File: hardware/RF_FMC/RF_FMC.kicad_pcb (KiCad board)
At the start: 4 copper layers, 84 x 69 mm, 32 parts, among them CN1 FMC_Mezzanine, Q1 SI1539CDL-T1-GE3, Q2 SI1539CDL-T1-GE3, Q3 SI1539CDL-T1-GE3, Q4 Si7141DP, Q5 Si7141DP, Q6 Si7141DP, U1 24LC024-I/SN

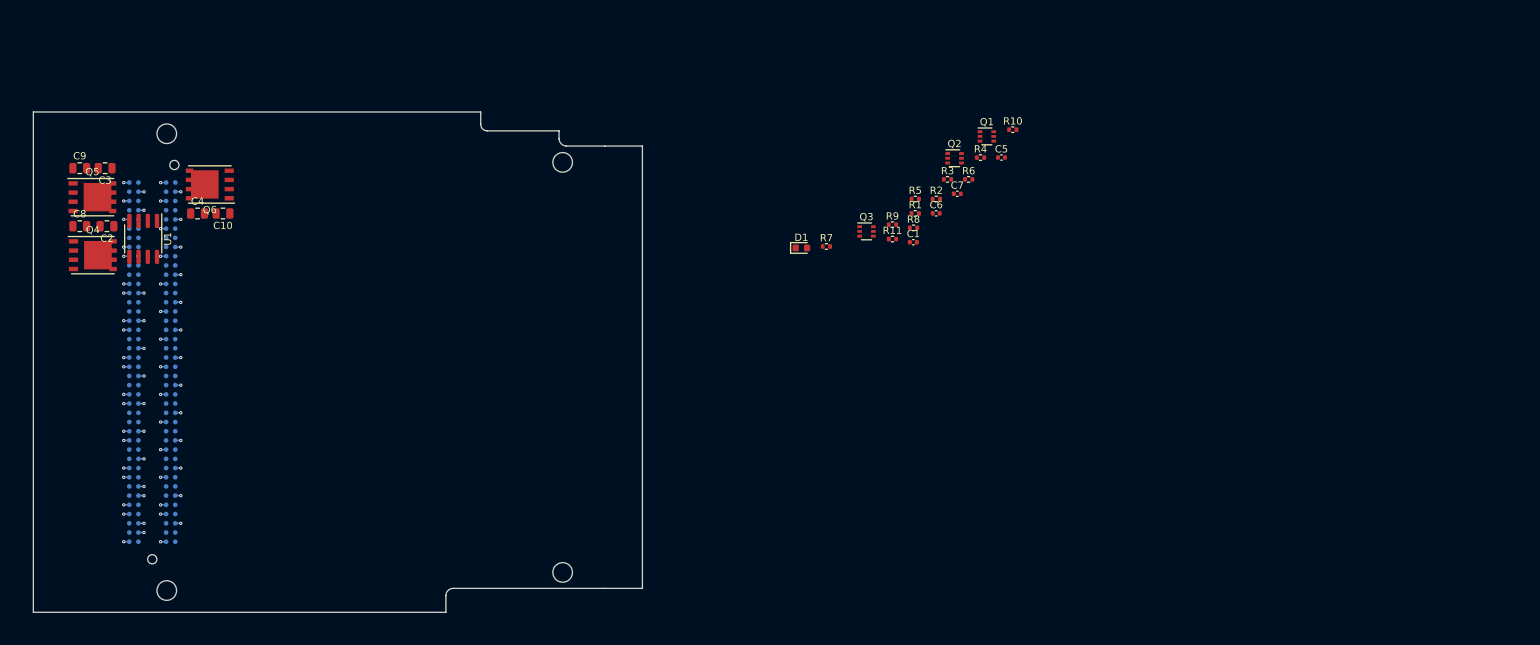
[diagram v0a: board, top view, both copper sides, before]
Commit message: Redid FMC template to parts I can actually buy!
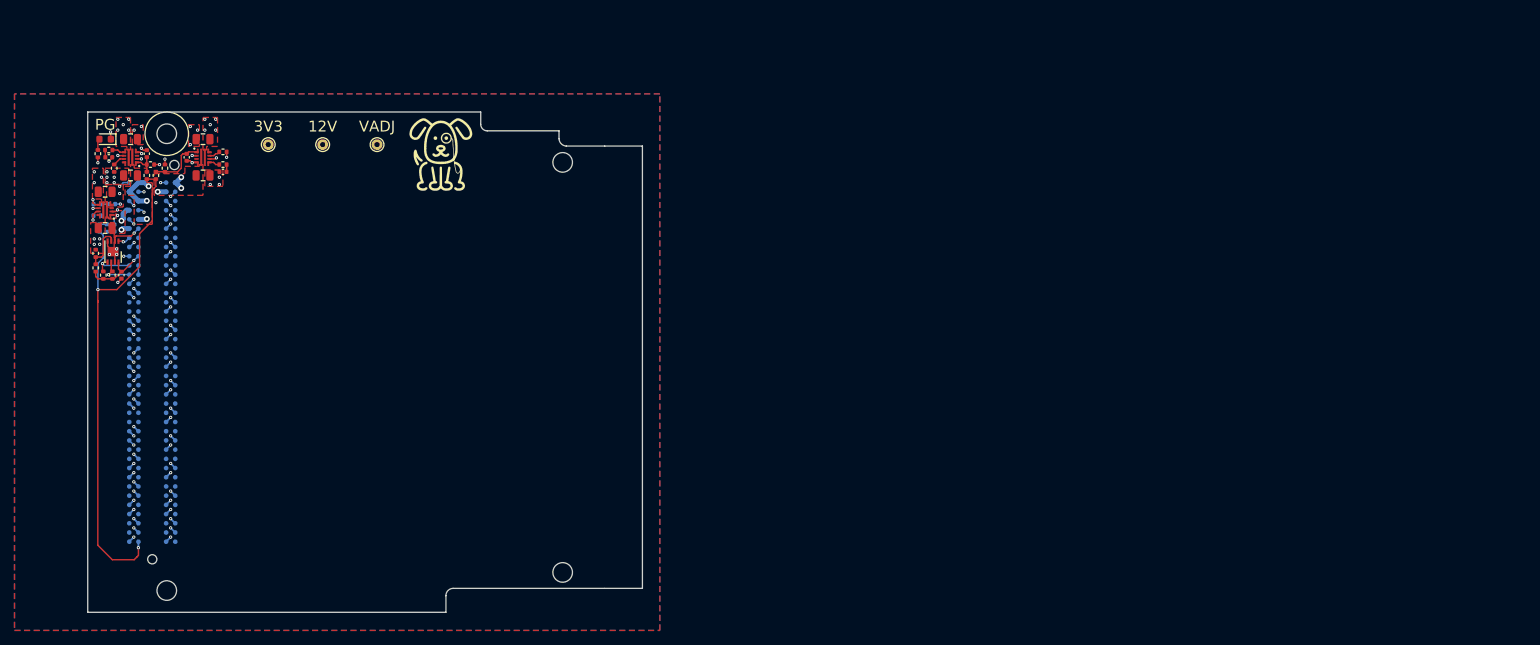
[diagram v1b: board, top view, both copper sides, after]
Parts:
- removed Q1, Q2, Q3: SI1539CDL-T1-GE3, Package_TO_SOT_SMD:SOT-363_SC-70-6
- removed Q4, Q5, Q6: Si7141DP, Package_SO:PowerPAK_SO-8_Single
- added C11: 10u, Capacitor_SMD:C_0805_2012Metric, F.Cu at (112.5, 76.5)
- added C12: 10u, Capacitor_SMD:C_0805_2012Metric, F.Cu at (116.0, 69.2)
- added C13: 10u, Capacitor_SMD:C_0805_2012Metric, F.Cu at (126.0, 69.2)
- added M1: Logo_10mmx10mm, Misc_WUT:Logo_10mmx10mm, F.Cu at (158.8, 71.5)
- added R12: 100, Resistor_SMD:R_0402_1005Metric, B.Cu at (111.4, 78.2)
- added R13: 100, Resistor_SMD:R_0402_1005Metric, F.Cu at (113.0, 70.8)
- added R14: 100, Resistor_SMD:R_0402_1005Metric, F.Cu at (128.8, 72.8)
- added R15: 2k, Resistor_SMD:R_0402_1005Metric, B.Cu at (111.4, 79.8)
- added R16: 2k, Resistor_SMD:R_0402_1005Metric, F.Cu at (113.8, 73.2)
- added R17: 2k, Resistor_SMD:R_0402_1005Metric, F.Cu at (128.8, 71.0)
- added TP1: TestPoint, TestPoint:TestPoint_THTPad_D1.5mm_Drill0.7mm, F.Cu at (142.5, 70.0)
- added TP2: TestPoint, TestPoint:TestPoint_THTPad_D1.5mm_Drill0.7mm, F.Cu at (135.0, 70.0)
- added TP3: TestPoint, TestPoint:TestPoint_THTPad_D1.5mm_Drill0.7mm, F.Cu at (150.0, 70.0)
- added U2: LM73100RPWR, IC_WUT:TI_LM73100_RPW, F.Cu at (112.5, 79.0)
- added U3: LM73100RPWR, IC_WUT:TI_LM73100_RPW, F.Cu at (116.0, 71.8)
- added U4: LM73100RPWR, IC_WUT:TI_LM73100_RPW, F.Cu at (126.0, 71.8)
- C10, C9: value 10u -> 10n; footprint Capacitor_SMD:C_0805_2012Metric -> Capacitor_SMD:C_0402_1005Metric
- C5, R6: moved to B.Cu
- C8: value 10u -> 10n; footprint Capacitor_SMD:C_0805_2012Metric -> Capacitor_SMD:C_0402_1005Metric; moved to B.Cu
- R10: value 10k -> 100k
- R11: value 1k -> 100k
- R8: value 10k -> 1k
- R9: value 10k -> 100k; moved to B.Cu
- U1: value 24LC024-I/SN -> 24LC02BT-I/MNY; footprint Package_SO:SOIC-8_3.9x4.9mm_P1.27mm -> Package_DFN_QFN:DFN-8-1EP_3x2mm_P0.5mm_EP1.3x1.5mm
- moved C5 122.8 mm to (113.8, 81.5), turned to -90 degrees
- moved R4 122.1 mm to (112.2, 88.0), turned to 90 degrees
- moved R6 120.0 mm to (111.8, 81.5), turned to 90 degrees
- moved R10 119.0 mm to (118.8, 72.8)
- moved R2 116.2 mm to (111.2, 85.0), turned to 90 degrees
- moved R3 115.9 mm to (113.5, 88.0), turned to 90 degrees
- moved R1 113.3 mm to (111.2, 87.0), turned to 90 degrees
- moved R5 112.9 mm to (111.5, 71.2), turned to 90 degrees
- moved C1 109.3 mm to (114.8, 88.0), turned to -90 degrees
- moved C6 109.2 mm to (118.2, 71.2), turned to 90 degrees
- moved R9 108.3 mm to (112.8, 81.5), turned to -90 degrees
- moved C7 106.4 mm to (123.8, 71.8), turned to -90 degrees
- moved R8 104.7 mm to (119.5, 74.2), turned to 90 degrees
- moved R11 100.8 mm to (120.8, 73.2), turned to 90 degrees
- moved D1 97.2 mm to (112.5, 69.2), turned to 180 degrees
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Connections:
- C10 pad 1: VADJ -> Net-(C10-Pad1)
- C8 pad 1: +12V -> Net-(C8-Pad1)
- C9 pad 1: +3V3 -> Net-(C9-Pad1)
- R10 pad 1: VADJ_FMC -> Net-(C6-Pad1)
- R10 pad 2: Net-(Q3-Pad6) -> GND
- R11 pad 1: +3V3 -> Net-(C7-Pad1)
- R11 pad 2: Net-(D1-Pad2) -> GND
- R5 pad 1: /PG_C2M -> +3V3
- R5 pad 2: Net-(C5-Pad1) -> Net-(D1-Pad2)
- R6 pad 2: Net-(C6-Pad1) -> Net-(C5-Pad1)
- R7 pad 2: Net-(C7-Pad1) -> Net-(C6-Pad1)
- R8 pad 1: 12V_FMC -> /PG_C2M
- R8 pad 2: Net-(Q1-Pad6) -> Net-(C7-Pad1)
- R9 pad 1: 3V3_FMC -> Net-(C5-Pad1)
- R9 pad 2: Net-(Q2-Pad6) -> GND
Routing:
- net /PG_C2M: track 0.00 -> 73.9 mm, vias 0 -> 2
- net GND: track 46.9 -> 73.9 mm, vias 61 -> 100
- net 3V3_AUX: track 0.00 -> 9.33 mm, vias 0 -> 1
- net Net-(C7-Pad1): track 0.00 -> 7.80 mm
- net 3V3_FMC: track 0.00 -> 7.56 mm, vias 0 -> 3
- net Net-(R1-Pad2): track 0.00 -> 6.15 mm
- net /FMC_SDA: track 0.00 -> 5.44 mm, vias 0 -> 1
- net /FMC_SCL: track 0.00 -> 4.94 mm, vias 0 -> 1
- net /GA1: track 0.00 -> 4.33 mm, vias 0 -> 1
- net Net-(C5-Pad1): track 0.00 -> 4.30 mm, vias 0 -> 1
- net Net-(C6-Pad1): track 0.00 -> 3.48 mm
- net VADJ_FMC: track 0.00 -> 3.44 mm, vias 0 -> 3
- net 12V_FMC: track 0.00 -> 3.27 mm, vias 0 -> 2
- net Net-(R15-Pad1): track 0.00 -> 2.30 mm, vias 0 -> 1
- net Net-(R12-Pad1): track 0.00 -> 1.96 mm, vias 0 -> 1
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- added copper zone on F.Cu, net +12V
- added copper zone on F.Cu, net +3V3
- added copper zone on F.Cu, net 12V_FMC
- added copper zone on F.Cu, net 3V3_FMC
- added copper zone on B.Cu, net GND
- added copper zone on F.Cu, net GND
- added copper zone on F.Cu, net VADJ
- added copper zone on F.Cu, net VADJ_FMC
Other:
- board size 84 x 69 mm -> 76.5 x 69 mm
- board text added: "12V"
- board text added: "3V3"
- board text added: "PG"
- board text added: "VADJ"

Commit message: Now working on FMC card from template
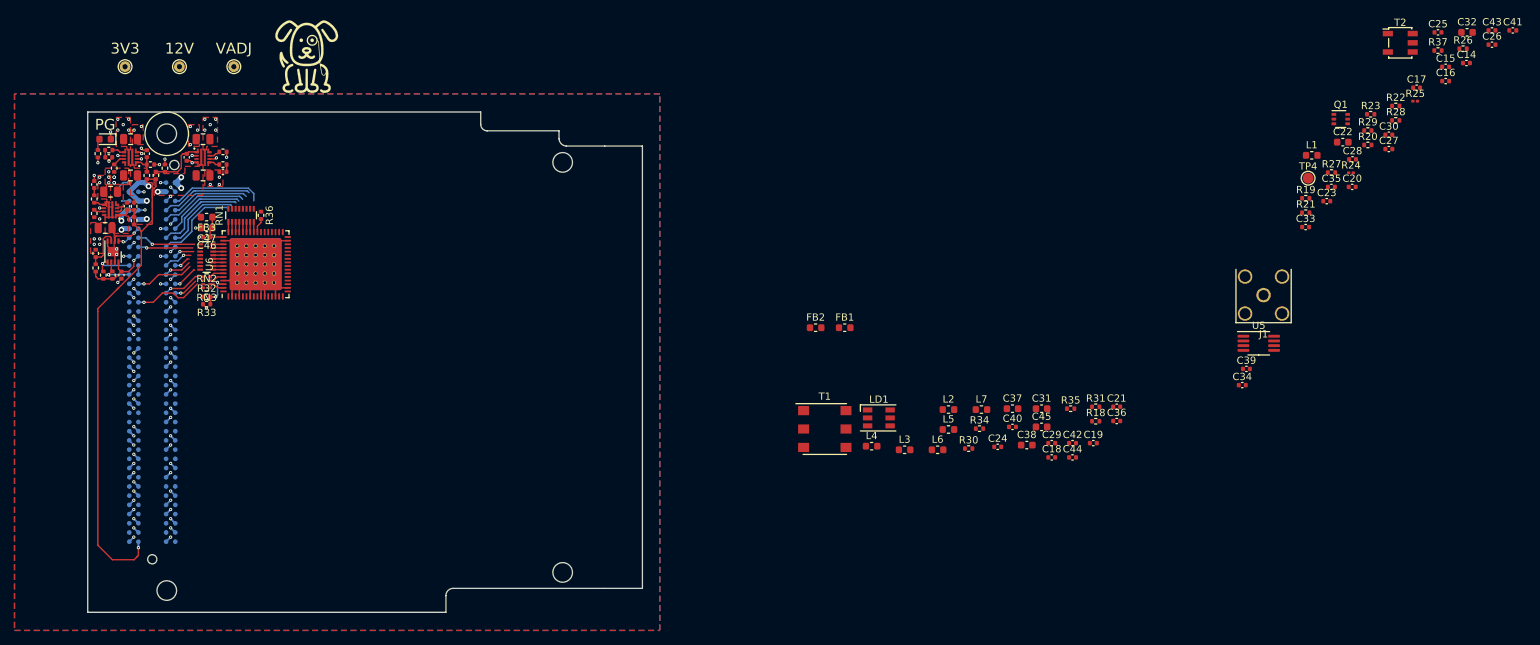
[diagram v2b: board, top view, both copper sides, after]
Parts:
- added C14: 100n, Capacitor_SMD:C_0402_1005Metric, F.Cu at (300.2, 58.8)
- added C15: 47p, Capacitor_SMD:C_0402_1005Metric, F.Cu at (297.4, 59.3)
- added C16: 22p, Capacitor_SMD:C_0402_1005Metric, F.Cu at (297.4, 61.2)
- added C17: 200p, Capacitor_SMD:C_0402_1005Metric, F.Cu at (293.4, 62.1)
- added C18: 150p, Capacitor_SMD:C_0402_1005Metric, F.Cu at (243.1, 113.1)
- added C19: 47p, Capacitor_SMD:C_0402_1005Metric, F.Cu at (248.8, 111.2)
- added C20: 8p2, Capacitor_SMD:C_0402_1005Metric, F.Cu at (284.5, 75.8)
- added C21: 200p, Capacitor_SMD:C_0402_1005Metric, F.Cu at (252.0, 106.2)
- added C22: 10u, Capacitor_SMD:C_0603_1608Metric, F.Cu at (283.2, 69.7)
- added C23: 22p, Capacitor_SMD:C_0402_1005Metric, F.Cu at (281.0, 77.8)
- added C24: 100n, Capacitor_SMD:C_0402_1005Metric, F.Cu at (235.6, 111.7)
- added C25: 1n, Capacitor_SMD:C_0402_1005Metric, F.Cu at (296.3, 54.5)
- added C26: 100n, Capacitor_SMD:C_0402_1005Metric, F.Cu at (303.8, 56.2)
- added C27: 100n, Capacitor_SMD:C_0402_1005Metric, F.Cu at (289.5, 70.6)
- added C28: 10n, Capacitor_SMD:C_0402_1005Metric, F.Cu at (284.5, 72.0)
- added C29: 100n, Capacitor_SMD:C_0402_1005Metric, F.Cu at (243.1, 111.2)
- added C30: 8p2, Capacitor_SMD:C_0402_1005Metric, F.Cu at (289.5, 68.6)
- added C31: 2u2, Capacitor_SMD:C_0603_1608Metric, F.Cu at (241.7, 106.4)
- added C32: 1u, Capacitor_SMD:C_0603_1608Metric, F.Cu at (300.3, 54.5)
- added C33: 100n, Capacitor_SMD:C_0402_1005Metric, F.Cu at (278.1, 81.4)
- added C34: 8p2, Capacitor_SMD:C_0402_1005Metric, F.Cu at (269.3, 103.2)
- added C35: 8p2, Capacitor_SMD:C_0402_1005Metric, F.Cu at (281.6, 75.8)
- added C36: 8p2, Capacitor_SMD:C_0402_1005Metric, F.Cu at (252.0, 108.1)
- added C37: 10u, Capacitor_SMD:C_0603_1608Metric, F.Cu at (237.6, 106.4)
- added C38: 10u, Capacitor_SMD:C_0603_1608Metric, F.Cu at (239.6, 111.4)
- added C39: 100n, Capacitor_SMD:C_0402_1005Metric, F.Cu at (269.9, 100.9)
- added C40: 1n, Capacitor_SMD:C_0402_1005Metric, F.Cu at (237.6, 108.9)
- added C41: 100n, Capacitor_SMD:C_0402_1005Metric, F.Cu at (306.6, 54.2)
- added C42: 100n, Capacitor_SMD:C_0402_1005Metric, F.Cu at (245.9, 111.2)
- added C43: 100n, Capacitor_SMD:C_0402_1005Metric, F.Cu at (303.8, 54.2)
- added C44: 100n, Capacitor_SMD:C_0402_1005Metric, F.Cu at (245.9, 113.1)
- added C45: 1u, Capacitor_SMD:C_0603_1608Metric, F.Cu at (241.7, 108.9)
- added C46: 100n, Capacitor_SMD:C_0402_1005Metric, F.Cu at (126.5, 82.8)
- added C47: 1u, Capacitor_SMD:C_0603_1608Metric, F.Cu at (126.5, 81.5)
- added FB1: FerriteBead_Small, Inductor_SMD:L_0603_1608Metric, F.Cu at (214.5, 95.2)
- added FB2: FerriteBead_Small, Inductor_SMD:L_0603_1608Metric, F.Cu at (210.5, 95.2)
- added FB3: FerriteBead_Small, Inductor_SMD:L_0603_1608Metric, F.Cu at (126.5, 80.0)
- added J1: Conn_Coaxial, Connector_WUT:SMA_Linx_CONSMA002-L-G_Horizontal, F.Cu at (272.3, 90.8)
- added L1: 220n, Inductor_SMD:L_0603_1608Metric, F.Cu at (278.9, 71.5)
- added L2: 24n, Inductor_SMD:L_0603_1608Metric, F.Cu at (228.8, 106.5)
- added L3: 330n, Inductor_SMD:L_0603_1608Metric, F.Cu at (222.8, 112.1)
- added L4: 560n, Inductor_SMD:L_0603_1608Metric, F.Cu at (218.2, 111.6)
- added L5: 330n, Inductor_SMD:L_0603_1608Metric, F.Cu at (228.8, 109.3)
- added L6: 24n, Inductor_SMD:L_0603_1608Metric, F.Cu at (227.3, 112.1)
- added L7: 220n, Inductor_SMD:L_0603_1608Metric, F.Cu at (233.4, 106.5)
- added LD1: LED_Cree_CLX6E-FKC, LED_SMD:LED_RGB_PLCC-6, F.Cu at (219.2, 107.7)
- added Q1: SI1539CDL-T1-GE3, Package_TO_SOT_SMD:SOT-363_SC-70-6, F.Cu at (282.9, 66.5)
- added R18: 10R, Resistor_SMD:R_0402_1005Metric, F.Cu at (249.1, 108.2)
- added R19: 10R, Resistor_SMD:R_0402_1005Metric, F.Cu at (278.1, 77.4)
- added R20: 35R, Resistor_SMD:R_0402_1005Metric, F.Cu at (286.6, 70.0)
- added R21: 35R, Resistor_SMD:R_0402_1005Metric, F.Cu at (278.1, 79.4)
- added R22: 5R1, Resistor_SMD:R_0402_1005Metric, F.Cu at (290.5, 64.7)
- added R23: 22k, Resistor_SMD:R_0402_1005Metric, F.Cu at (287.0, 65.8)
- added R24: 51R, Resistor_SMD:R_0201_0603Metric, F.Cu at (284.3, 73.9)
- added R25: 51R, Resistor_SMD:R_0201_0603Metric, F.Cu at (293.2, 64.0)
- added R26: 5R1, Resistor_SMD:R_0402_1005Metric, F.Cu at (299.8, 56.8)
- added R27: 5R1, Resistor_SMD:R_0402_1005Metric, F.Cu at (281.6, 73.8)
- added R28: 5R1, Resistor_SMD:R_0402_1005Metric, F.Cu at (290.5, 66.7)
- added R29: 5R1, Resistor_SMD:R_0402_1005Metric, F.Cu at (286.6, 68.1)
- added R30: 10k, Resistor_SMD:R_0402_1005Metric, F.Cu at (231.6, 111.9)
- added R31: 100R, Resistor_SMD:R_0402_1005Metric, F.Cu at (249.1, 106.2)
- added R32: 5k1, Resistor_SMD:R_0402_1005Metric, F.Cu at (126.5, 91.0)
- added R33: 10k, Resistor_SMD:R_0402_1005Metric, F.Cu at (126.5, 92.0)
- added R34: 0, Resistor_SMD:R_0402_1005Metric, F.Cu at (233.1, 109.2)
- added R35: 10k, Resistor_SMD:R_0402_1005Metric, F.Cu at (245.7, 106.4)
- added R36: 33, Resistor_SMD:R_0402_1005Metric, F.Cu at (134.0, 79.8)
- added R37: 33, Resistor_SMD:R_0402_1005Metric, F.Cu at (296.3, 57.0)
- added RN1: 33, Resistor_SMD:R_Array_Convex_8x0602, F.Cu at (131.2, 79.8)
- added RN2: 33, Resistor_SMD:R_Array_Convex_8x0602, F.Cu at (126.5, 85.5)
- added RN3: 33, Resistor_SMD:R_Array_Convex_4x0402, F.Cu at (126.5, 89.0)
- added T1: PWB2010L, Transformer_WUT:Coilcraft_PWB, F.Cu at (211.8, 109.2)
- added T2: Macom_ETC1-1-13, Transformer_SMD:Transformer_MACOM_SM-22, F.Cu at (291.1, 56.0)
- added TP4: TestPoint, TestPoint:TestPoint_Pad_D1.5mm, F.Cu at (278.4, 74.6)
- added U5: REF5025IDGK, Package_SO:MSOP-8_3x3mm_P0.65mm, F.Cu at (271.6, 97.4)
- added U6: LTC2216, IC_WUT:QFN-64-1EP_9x9mm_P0.5mm_EP7.15x7.15mm, F.Cu at (133.2, 86.5)
- C5, C8, R12, R15, R6, R9: moved to F.Cu
- moved M1 22.9 mm to (140.2, 58.0)
- moved TP1 22.5 mm to (122.8, 59.2)
- moved TP2 22.5 mm to (115.2, 59.2)
- moved TP3 22.5 mm to (130.2, 59.2)
- moved R6 4.85 mm to (116.5, 80.5)
- moved R9 4.80 mm to (116.5, 78.5), turned to 90 degrees
- moved C8 3.61 mm to (111.0, 75.5), turned to 90 degrees
- moved C5 3.47 mm to (115.5, 78.5), turned to 90 degrees
- moved R12 0.81 mm to (111.0, 77.5), turned to 90 degrees
- moved C11 0.75 mm to (113.2, 76.5)
- moved U2 0.75 mm to (113.2, 79.0)
- moved R15 0.50 mm to (111.0, 79.5), turned to -90 degrees
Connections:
- net /FMC_SCL renamed /FMC Connector/FMC_SCL
- net /FMC_SDA renamed /FMC Connector/FMC_SDA
- net /GA0 renamed /FMC Connector/GA0
- net /GA1 renamed /FMC Connector/GA1
- net /PG_C2M renamed /FMC Connector/PG_C2M
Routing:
- net (no net): track 0.00 -> 153.6 mm, vias 0 -> 11
- net GND: track 73.9 -> 127.2 mm, vias 100 -> 98
- net /FMC Connector/PG_C2M: track 73.9 -> 65.3 mm, vias 2 -> 1
- net +3V3: track 0.74 -> 9.20 mm
- net Net-(R32-Pad2): track 0.00 -> 4.76 mm, vias 0 -> 2
- net OVDD: track 0.00 -> 4.71 mm
- net Net-(RN3-Pad4): track 0.00 -> 2.02 mm
- net Net-(RN3-Pad3): track 0.00 -> 2.02 mm
- net Net-(R35-Pad1): track 0.00 -> 2.02 mm
- net Net-(R36-Pad2): track 0.00 -> 2.01 mm
- net Net-(RN2-Pad8): track 0.00 -> 1.41 mm
- net Net-(RN2-Pad7): track 0.00 -> 1.41 mm
- net Net-(RN2-Pad6): track 0.00 -> 1.41 mm
- net Net-(RN2-Pad5): track 0.00 -> 1.41 mm
- net Net-(RN2-Pad4): track 0.00 -> 1.41 mm
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
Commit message: Started on ADC layout
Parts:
- removed the C16 at (297.4, 61.2)
- removed the C17 at (293.4, 62.1)
- removed the C23 at (281.0, 77.8)
- removed the C26 at (303.8, 56.2)
- removed the C27 at (289.5, 70.6)
- removed the L1 at (278.9, 71.5)
- removed the L2 at (228.8, 106.5)
- removed L4: 560n, Inductor_SMD:L_0603_1608Metric
- removed L6: 24n, Inductor_SMD:L_0603_1608Metric
- removed L7: 220n, Inductor_SMD:L_0603_1608Metric
- removed T1: PWB2010L, Transformer_WUT:Coilcraft_PWB
- removed T2: Macom_ETC1-1-13, Transformer_SMD:Transformer_MACOM_SM-22
- removed TP4: TestPoint, TestPoint:TestPoint_Pad_D1.5mm
- added H3: Shield, Shield_WUT:Shield_Masach_MS477-10_47.7x18.2x4mm_TH.step, F.Cu at (146.2, 117.7)
- added R1: R, Resistor_SMD:R_0402_1005Metric, F.Cu at (203.5, 112.5)
- added TR1: ETC1-1T-2TR, Transformer_WUT:Macom_ETC-1xx, F.Cu at (146.8, 116.5)
- added TR2: ETC1-1T-2TR, Transformer_WUT:Macom_ETC-1xx, F.Cu at (146.8, 111.8)
- C20: value 8p2 -> 100n
- C21: value 200p -> 100n
- C36: renamed from C41; moved to B.Cu
- C37: renamed from C42; moved to B.Cu
- C38: renamed from C43; moved to B.Cu
- C40: renamed from C45; moved to B.Cu
- R25: renamed from R24; footprint Resistor_SMD:R_0201_0603Metric -> Resistor_SMD:R_0402_1005Metric
- R26: renamed from R25; footprint Resistor_SMD:R_0201_0603Metric -> Resistor_SMD:R_0402_1005Metric
- R32: renamed from R31; footprint Resistor_SMD:R_0402_1005Metric -> Resistor_SMD:R_0201_0603Metric
- moved C36 180.9 mm to (137.2, 117.5), turned to 180 degrees
- moved C38 176.4 mm to (137.2, 112.5), turned to 180 degrees
- moved R27 171.7 mm to (139.0, 117.0)
- moved C27 169.6 mm to (144.5, 121.5)
- moved C22 162.8 mm to (149.0, 123.8), turned to 90 degrees
- moved R29 156.8 mm to (140.5, 112.5), turned to 90 degrees
- moved R26 156.8 mm to (143.5, 110.8), turned to 90 degrees
- moved R23 156.4 mm to (143.9, 119.2)
- moved C25 155.6 mm to (141.5, 116.5), turned to 90 degrees
- moved R30 153.7 mm to (139.5, 112.5), turned to 90 degrees
- moved C14 152.6 mm to (159.5, 117.8)
- moved R21 151.1 mm to (143.0, 117.0)
- moved C15 151.0 mm to (158.0, 117.2), turned to 90 degrees
- moved R28 148.7 mm to (139.0, 116.0)
- moved C30 146.6 mm to (140.5, 115.5), turned to 90 degrees
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- renumbered C18 to C16, C19 to C17, C22 to C18, C24 to C19, C25 to C22, C28 to C23, C29 to C24, C30 to C25, C31 to C26, C32 to C27, C33 to C28, C34 to C29, C35 to C30, C36 to C31, C37 to C32, C38 to C33, C39 to C34, C40 to C35, C44 to C39, C46 to C41, C47 to C42, L3 to L1, L5 to L2, R9 to R10, R10 to R11, R11 to R12, R12 to R13, R13 to R14, R14 to R15, R15 to R16, R16 to R17, R17 to R18, R18 to R19, R1 to R2, R19 to R20, R20 to R21, R21 to R22, R22 to R23, R23 to R24, R26 to R27, R27 to R28, R28 to R29, R2 to R3, R29 to R30, R30 to R31, R32 to R33, R33 to R34, R34 to R35, R35 to R36, R36 to R37, R37 to R38, R3 to R4, R4 to R5, R5 to R6, R6 to R7, R7 to R8, R8 to R9
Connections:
- net Net-(R29-Pad1) renamed /Direct Sampling ADC/ENC_N
- C20 pad 1: Net-(C20-Pad1) -> /Direct Sampling ADC/ADC_P
- C21 pad 1: Net-(C20-Pad1) -> /Direct Sampling ADC/ADC_N
- C21 pad 2: GND -> Net-(C21-Pad2)
- R29 pad 1: Net-(R28-Pad1) (its old number) -> /Direct Sampling ADC/ENC_P
- R32 pad 1: Net-(R28-Pad1) (its old number) -> /Direct Sampling ADC/ENC_P
- U6 pad 12: Net-(R28-Pad1) (its old number) -> /Direct Sampling ADC/ENC_P
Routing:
- net (no net): track 153.6 -> 0.00 mm, vias 11 -> 0
- net GND: track 127.2 -> 141.8 mm, vias 98 -> 143
- net /FMC Connector/LA32_N: track 0.00 -> 12.9 mm
- net /FMC Connector/LA31_N: track 0.00 -> 12.8 mm
- net /FMC Connector/LA33_N: track 0.00 -> 12.6 mm
- net OVDD: track 4.71 -> 17.3 mm, vias 0 -> 2
- net /FMC Connector/LA33_P: track 0.00 -> 12.0 mm
- net /FMC Connector/LA31_P: track 0.00 -> 11.9 mm
- net /FMC Connector/LA30_N: track 0.00 -> 11.0 mm
- net /FMC Connector/LA32_P: track 0.00 -> 10.9 mm
- net /FMC Connector/LA30_P: track 0.00 -> 10.6 mm
- net VDD: track 0.00 -> 10.2 mm, vias 0 -> 4
- net /FMC Connector/LA26_N: track 0.00 -> 9.71 mm, vias 0 -> 1
- net Net-(C23-Pad2): track 0.00 -> 8.44 mm
- net unconnected-(CN1-PadD34): track 0.00 -> 8.12 mm, vias 0 -> 1
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
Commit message: Pc upgrade
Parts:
- R36: moved to B.Cu
- moved R38 170.7 mm to (134.2, 110.8)
- moved R36 111.6 mm to (135.5, 124.5), turned to -90 degrees
- moved C35 99.7 mm to (138.8, 121.2), turned to -90 degrees
- moved R35 96.9 mm to (136.2, 110.8), turned to 180 degrees
- moved FB2 82.7 mm to (129.2, 110.5), turned to 180 degrees
- moved C34 1.82 mm to (140.2, 120.8), turned to 0 degrees
- moved C33 1.12 mm to (140.2, 122.8)
- moved C32 0.79 mm to (140.5, 125.0)
- moved R31 0.71 mm to (141.5, 123.0)
- moved C27 0.10 mm to (144.6, 121.5)
- turned Q1 to 90 degrees
- turned R24 to 90 degrees
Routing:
- net GND: track 141.8 -> 144.6 mm, vias 143 -> 153
- net Net-(R36-Pad1): track 2.02 -> 4.47 mm, vias 0 -> 1
- net Net-(R35-Pad2): track 0.00 -> 1.41 mm
- net /Direct Sampling ADC/ADC_Dither: track 0.00 -> 1.41 mm
- net Net-(C33-Pad1): track 4.53 -> 5.69 mm
- net Net-(C32-Pad1): track 3.58 -> 4.16 mm
